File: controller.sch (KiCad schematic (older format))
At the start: 49 parts

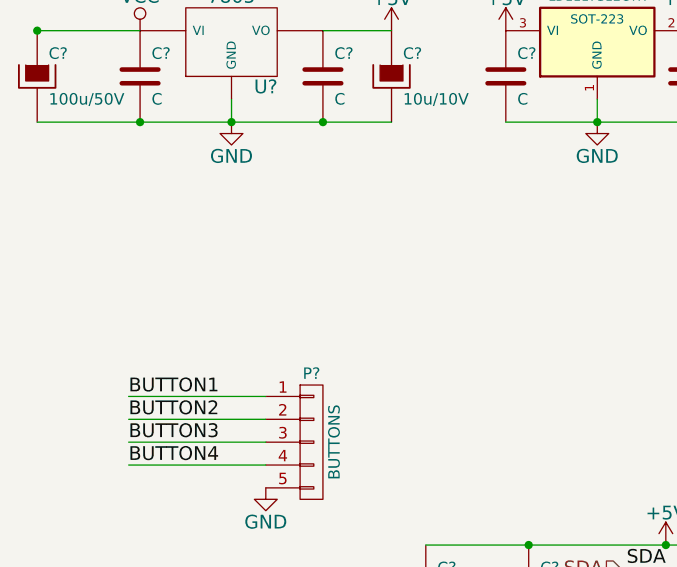
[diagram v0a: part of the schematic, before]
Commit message: Add ISP header
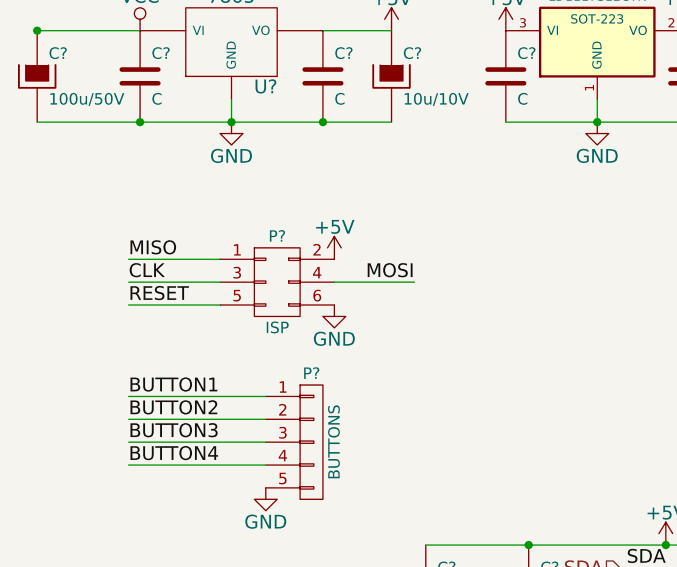
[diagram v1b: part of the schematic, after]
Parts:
- added P?: ISP, symbol CONN_02X03
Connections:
- net +5V: now also P?.2 (P2)
- net CLK: now also P?.3 (P3)
- net GND: now also P?.6 (P6)
- net MISO: now also P?.1 (P1)
- net MOSI: now also P?.4 (P4)
- new net RESET: P?.5 (P5)
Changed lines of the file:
@@
 Text Label 4350 2600 2    60   ~ 0
 BUTTON4
+$Comp
+L CONN_02X03 P?
+U 1 1 54E71E3F
+P 1700 5400
+F 0 "P?" H 1700 5600 50  0000 C CNN
+F 1 "ISP" H 1700 5200 50  0000 C CNN
+F 2 "" H 1700 4200 60  0000 C CNN
+F 3 "" H 1700 4200 60  0000 C CNN
+	1    1700 5400
+	1    0    0    -1
+$EndComp
+$Comp
+L +5V #PWR?
+U 1 1 54E72298
+P 1950 5300
+F 0 "#PWR?" H 1950 5150 60  0001 C CNN
+F 1 "+5V" H 1950 5440 60  0000 C CNN
+F 2 "" H 1950 5300 60  0000 C CNN
+F 3 "" H 1950 5300 60  0000 C CNN
+	1    1950 5300
+	1    0    0    -1
+$EndComp
+$Comp
+L GND #PWR?
+U 1 1 54E724FB
+P 1950 5500
+F 0 "#PWR?" H 1950 5250 60  0001 C CNN
+F 1 "GND" H 1950 5350 60  0000 C CNN
+F 2 "" H 1950 5500 60  0000 C CNN
+F 3 "" H 1950 5500 60  0000 C CNN
+	1    1950 5500
+	1    0    0    -1
+$EndComp
+Wire Wire Line
+	1950 5400 2300 5400
+Wire Wire Line
+	1450 5300 1050 5300
+Wire Wire Line
+	1450 5400 1050 5400
+Wire Wire Line
+	1450 5500 1050 5500
+Text Label 1050 5300 0    60   ~ 0
+MISO
+Text Label 1050 5400 0    60   ~ 0
+CLK
+Text Label 1050 5500 0    60   ~ 0
+RESET
+Text Label 2300 5400 2    60   ~ 0
+MOSI
 $EndSCHEMATC

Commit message: Add annotations and netlist
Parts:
- gave numbers to parts that had none: 47

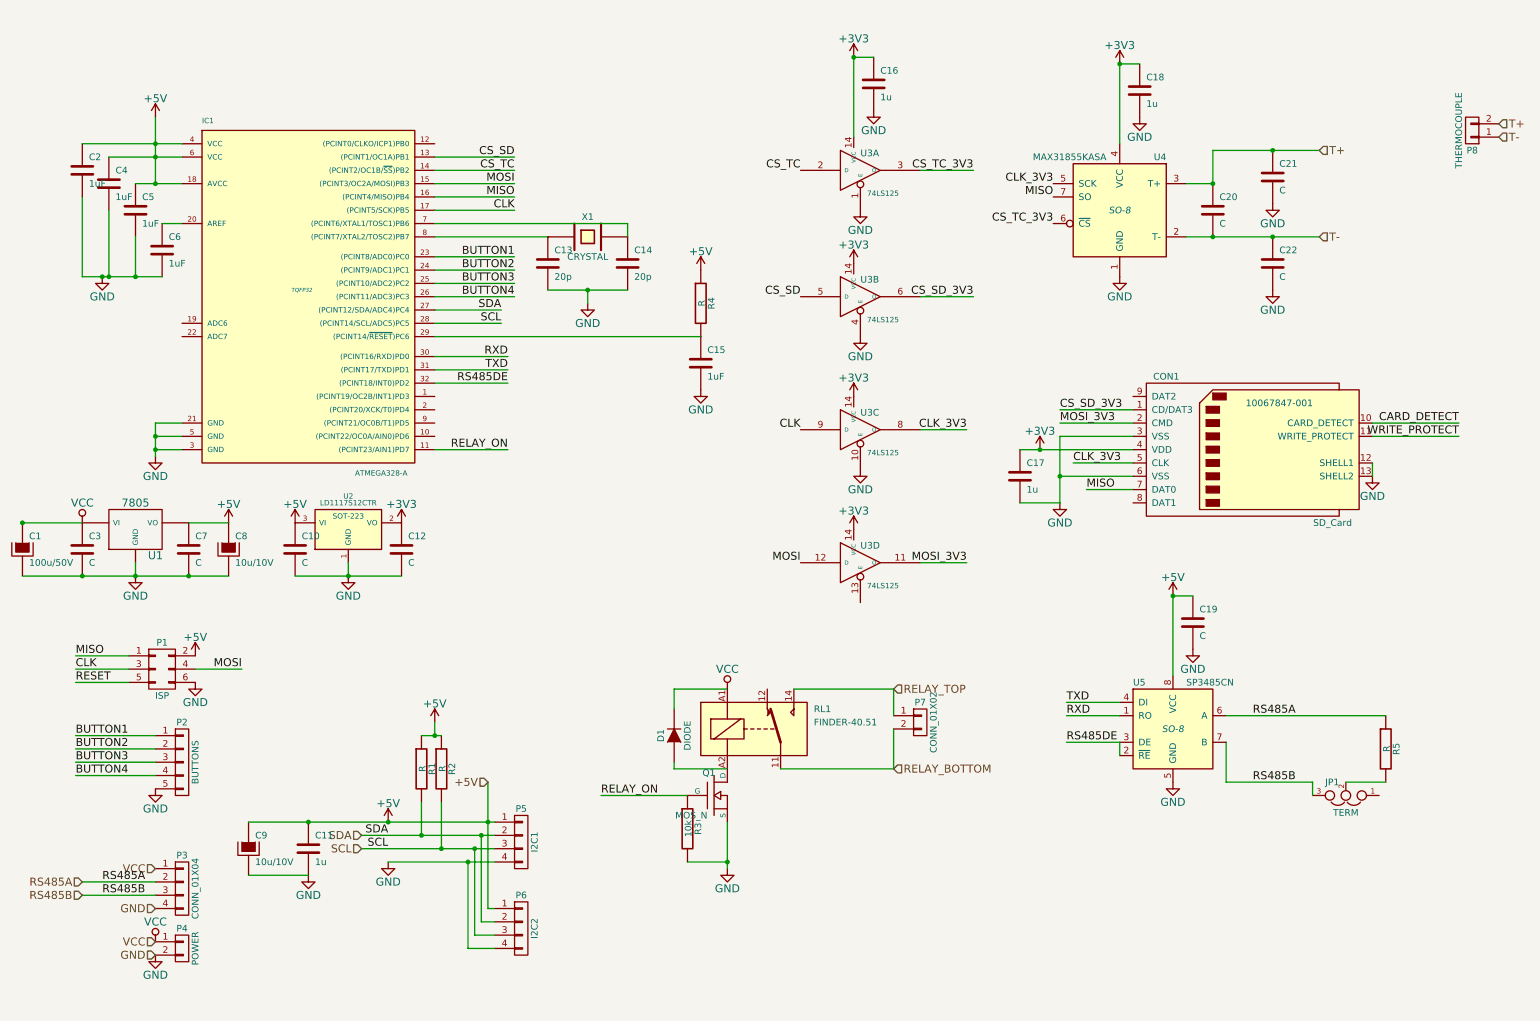
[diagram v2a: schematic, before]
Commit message: Add open drain output, shuffle other connectors around
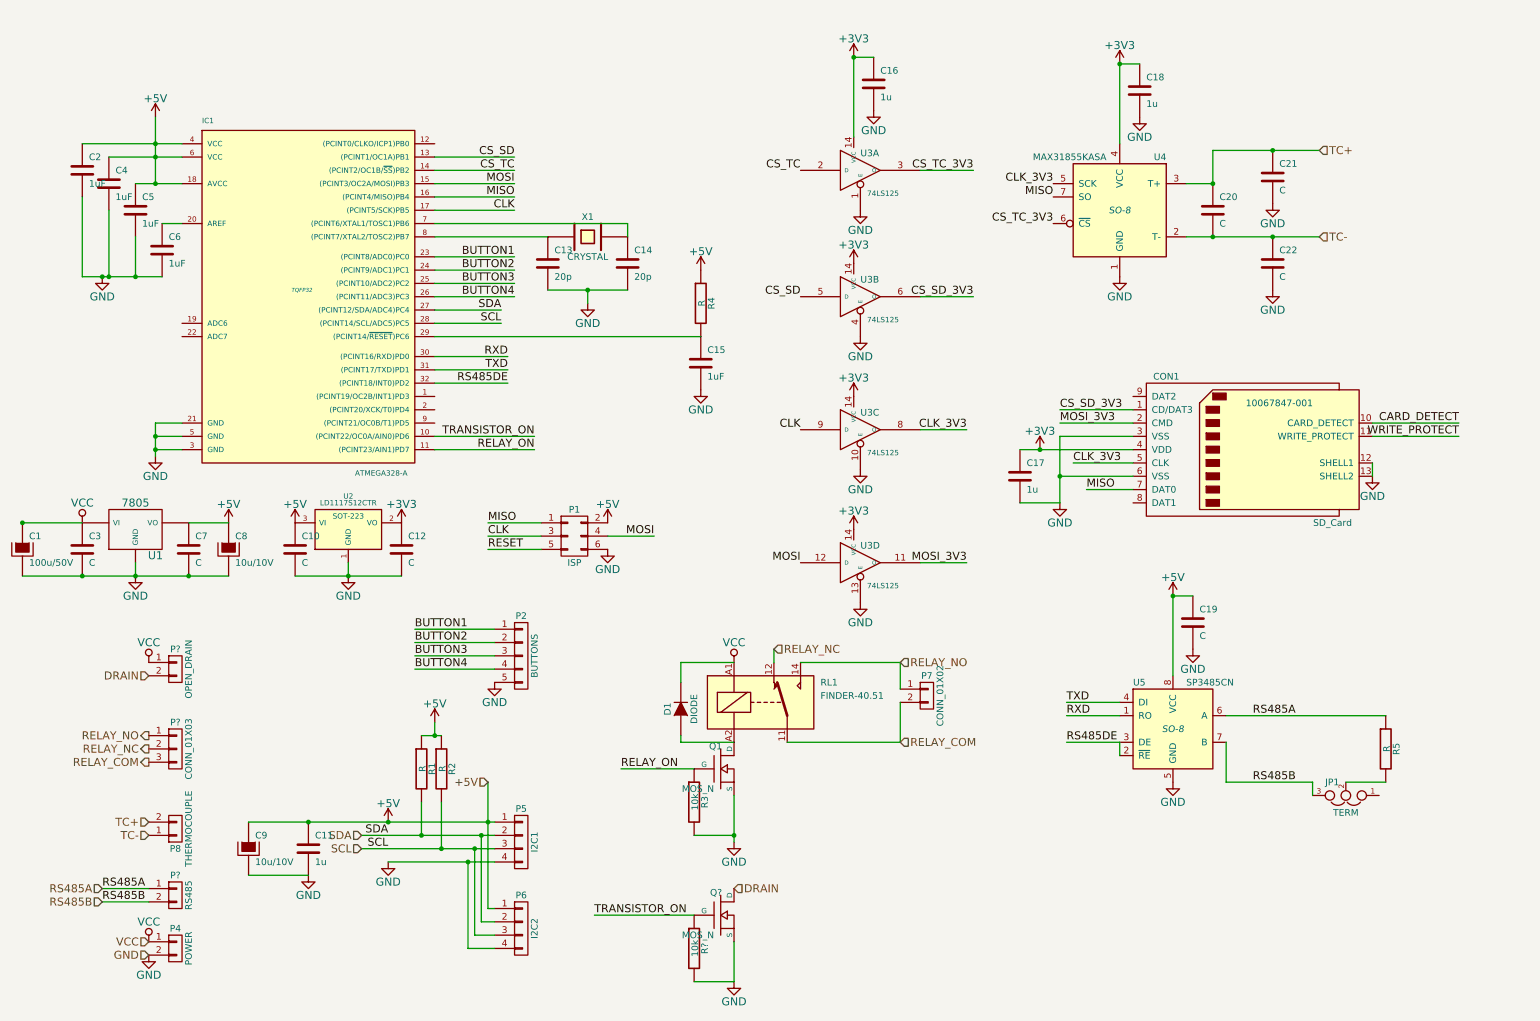
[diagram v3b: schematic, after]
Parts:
- removed P3: CONN_01X04, symbol CONN_01X04
- added P?: CONN_01X03, symbol CONN_01X03
- added P?: RS485, symbol CONN_01X02
- added P?: OPEN_DRAIN, symbol CONN_01X02
- added Q?: MOS_N, symbol MOS_N
- added R?: 10k, symbol R
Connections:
- net GND: now also U3.13 (E), Q?.S, R?.2
- net RS485A: now also P?.1 (P1)
- net RS485B: now also P?.2 (P2)
- net VCC: now also P?.1 (P1)
- net TRANSISTOR_ON: now reaches IC1.10 ((PCINT22/OC0A/AIN0)PD6)
- net TRANSISTOR_ON: now also Q?.G, R?.1
- net RELAY_NC: now reaches RL1.12
- net RELAY_NC: now also P?.2 (P2)
- net RELAY_BOTTOM renamed RELAY_COM
- net RELAY_COM: now also P?.3 (P3)
- net RELAY_TOP renamed RELAY_NO
- net RELAY_NO: now also P?.1 (P1)
- net T+ renamed TC+
- net T- renamed TC-
- new net DRAIN: P?.2 (P2), Q?.D
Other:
- moved on the sheet: D1, P1, P2, P4, P7, P8, Q1, R3, RL1

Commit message: Shuffle stuff around, generate the new schematics svg
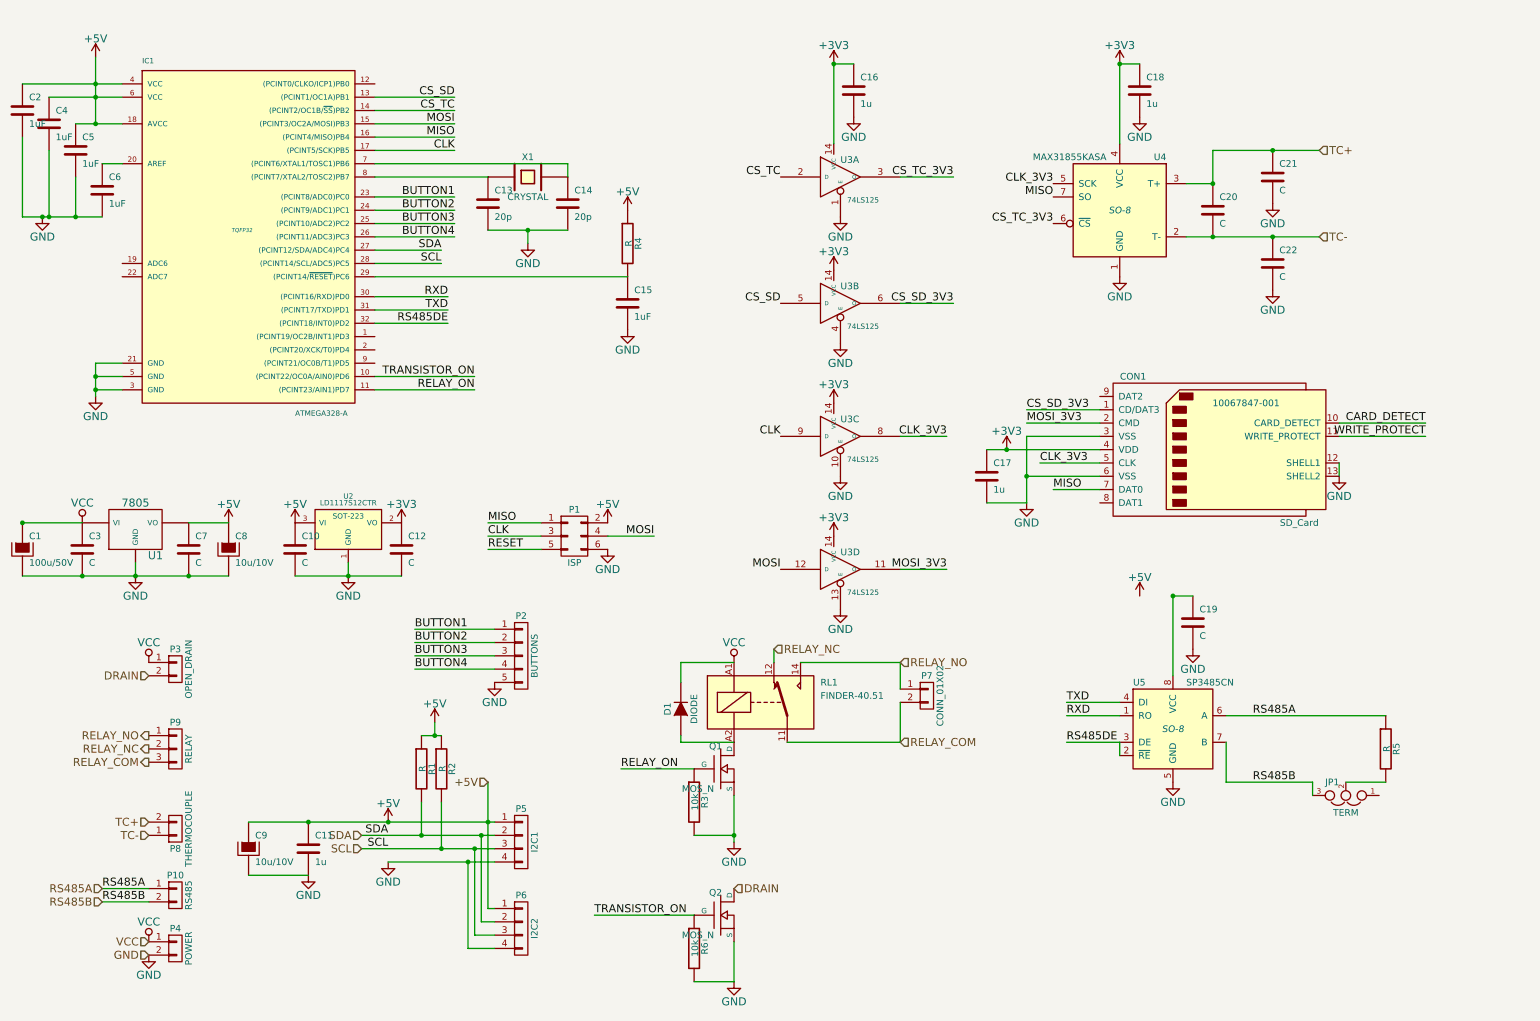
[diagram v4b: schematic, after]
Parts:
- P9: renamed from P?; value CONN_01X03 -> RELAY
- gave numbers to parts that had none: 4
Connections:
- net +5V: no longer C19.1, U5.8 (VCC)
- new net: C19.1, U5.8 (VCC)
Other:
- moved on the sheet: C13, C14, C15, C16, C17, C2, C4, C5, C6, CON1, IC1, R4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

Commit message: Add netlist, assign footprints and 3d models, fool around with placement a bit
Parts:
- removed P7: CONN_01X02, symbol CONN_01X02
- C1: footprint (none) -> Capacitors_ThroughHole:Capacitor8x13RM3.8
- C10, C11, C12, C13, C14, C15, C16, C17, C18, C19, C2, C20, C21, C22, C3, C4, C5, C6, C7: footprint (none) -> Capacitors_SMD:C_0603_HandSoldering
- C8, C9: footprint (none) -> Capacitors_ThroughHole:Capacitor5x6RM2.5
- CON1: footprint 10067847-001 -> Connect:SD_Card_Receptacle
- D1: footprint (none) -> Diodes_SMD:Diode-SMA_Handsoldering
- IC1: footprint TQFP32 -> Housings_QFP:TQFP-32_7x7mm_Pitch0.8mm
- JP1: footprint (none) -> Pin_Arrays:pin_array_1x03
- P1: footprint (none) -> Pin_Arrays:pin_array_2x03
- P10, P3, P4, P8: footprint (none) -> w_conn_screw:mors_2p
- P2: footprint (none) -> Pin_Headers:Pin_Header_Straight_1x05
- P5, P6: footprint (none) -> Pin_Headers:Pin_Header_Straight_1x04
- P9: footprint (none) -> w_conn_screw:mors_3p
- Q1: footprint (none) -> Transistors_SMD:sot23
- Q2: footprint (none) -> Transistors_TO-220:TO-220_FET-GDS_Vertical_LargePads
- R1, R2, R3, R4, R5, R6: footprint (none) -> Resistors_SMD:R_0603_HandSoldering
- RL1: footprint (none) -> Relays_ThroughHole:Relay_DPDT_Schrack-RT2_RM5mm
- U1: footprint (none) -> Discret:LM78XXV
- U2: footprint SOT-223 -> SMD_Packages:SOT-223
- U3: footprint (none) -> Housings_SOIC:SOIC-14_3.9x8.7mm_Pitch1.27mm
- U4, U5: footprint SO-8 -> Housings_SOIC:SOIC-8_3.9x4.9mm_Pitch1.27mm
- X1: footprint (none) -> Crystals:Crystal_HC49-SD_SMD
